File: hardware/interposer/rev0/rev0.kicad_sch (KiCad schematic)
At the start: 14 parts, among them J1 Z80_PLUG_TO_MB, J2 Z80_SOCKET_CPU, J3 5V_INPUT, U1 74AHCT165, U2 74AHCT165, U3 74AHCT165, U4 74AHCT165, U5 PICO_2_W

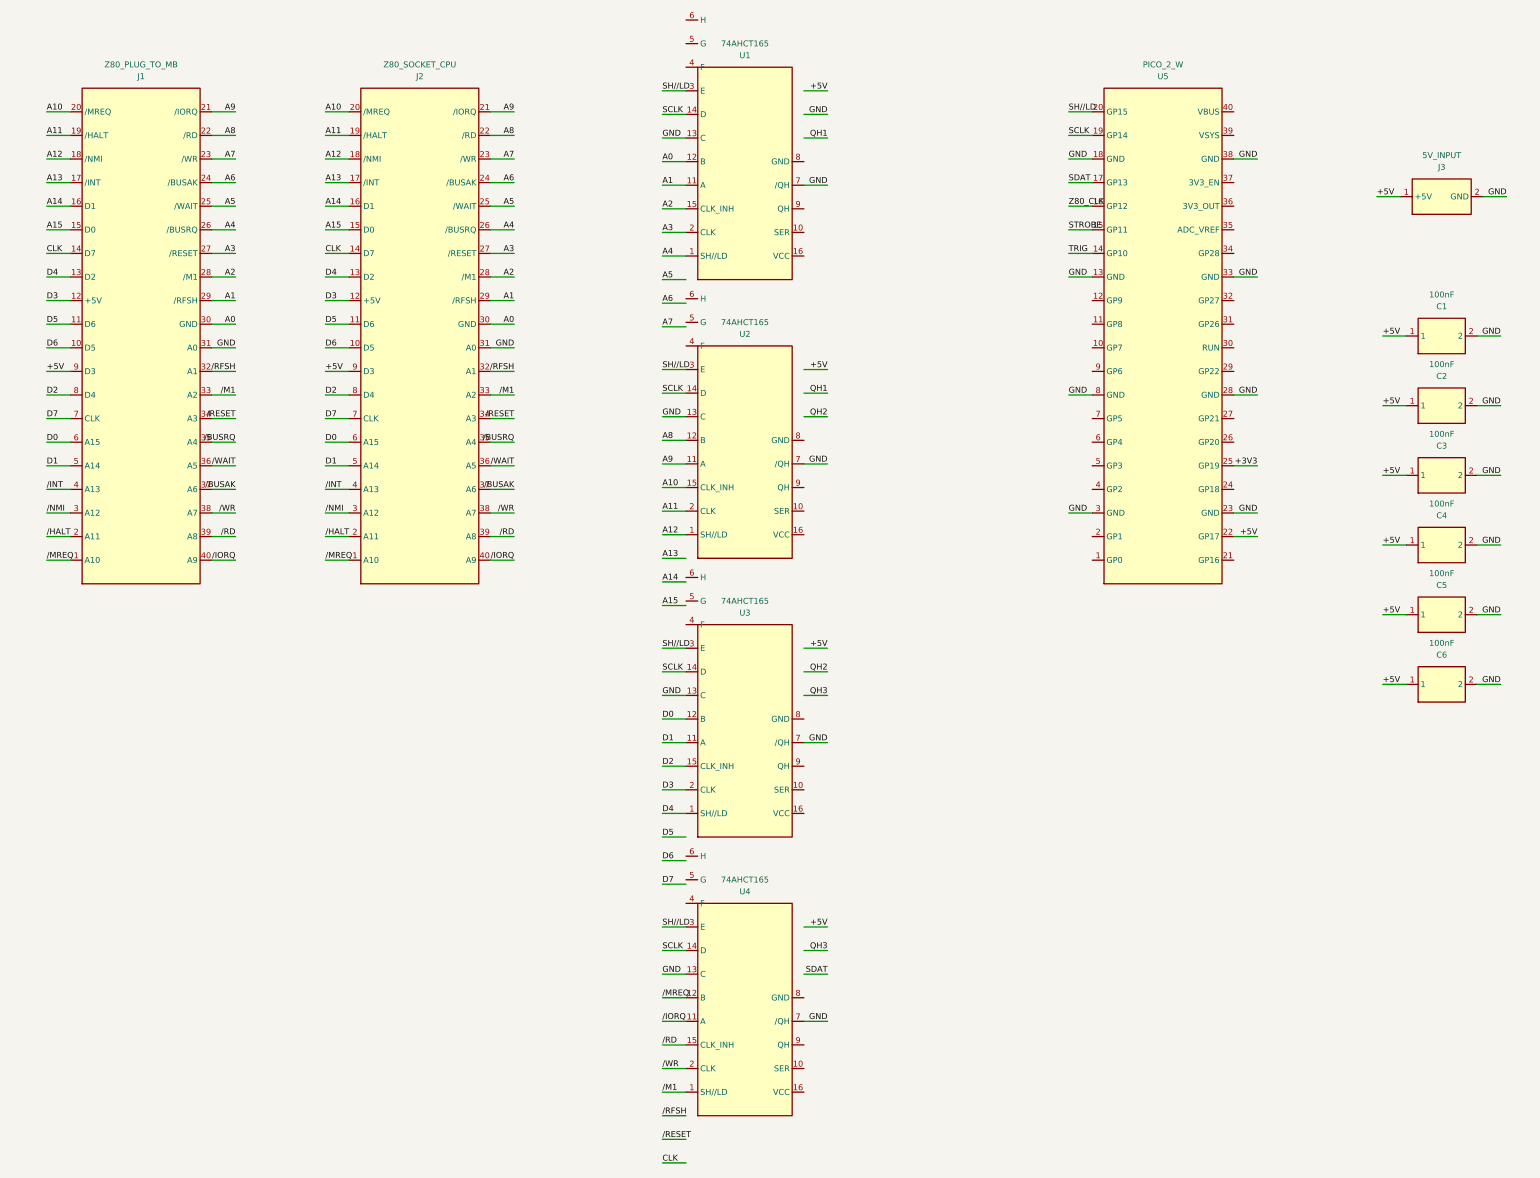
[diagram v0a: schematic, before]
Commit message: hardware: fix mirrored pin placement in interposer schematic generators
The reva/rev0 generators placed a symbol pin at (x + px, y + py), but KiCad
stores symbol geometry Y-up while the sheet is Y-down, so the pin actually
lands at (x + px, y - py).  Every wire stub and net label was therefore
attached to the mirror-image pin and the netlist was broken: reva ERC
reported 93 errors (85 pin_not_connected + 8 label_dangling), rev0 58.

- reva/rev0: correct the Y transform in place(), and make Symbol.pin_pos()/
anchor() use `+hh - off` so `off` really counts down from the top of the box
  (the 'T'/'B' sides were inverted too).  Label justification flipped so the
  text runs away from the symbol body, as in the floppy-adapter generator.
- reva: the 595 drive chain is FOUR devices (U3/U4/U5/U15 -- see SR_OUT), but
  the 165 capture chain also started at y=205, putting U6 directly on top of
  U15.  That shorted SR_RCK/GND, /OE_ADDR/A0, +5V/A1, +5V/A2 and GND/A3 -- the
  netlist reported GND as "A3" with 47 nodes.  Capture chain now starts at 260.
- reva/rev0: snap symbol origins to the 1.27 mm connection grid, and size the
  Z84C00 body 111.76 mm (44 x 1.27) so its pins land on grid.  Verified
  electrically neutral: the exported netlist (nets section) is byte-identical
  with and without the snap.
- reva: fix a stale docstring that claimed to be the Rev 0 generator.

ERC: reva 93 -> 12 errors (565 -> 51 violations), rev0 58 -> 28 (286 -> 46).
The 12/28 remaining are genuinely unused pins (U7/U8 /QH, U11 2A2/2Y2, Pico
RUN/ADC_VREF/3V3_EN/VBUS, ESP32-C3 IO2/IO8/IO10), not geometry faults.  The
residual warnings are `endpoint_off_grid`-free now; what is left is
lib_symbol_issues (no 'local' entry in sym-lib-table -- the symbols are
embedded, so it is cosmetic) and isolated_pin_label on nets that are real
design gaps (/MREQ_DRV, /IORQ_RAW, /Z80_CLK, /ESP_EN, /ESP_BOOT).

Note: gen_lff_sch.py is unaffected -- it emits hierarchical sheets, no pins.

Refs #62.
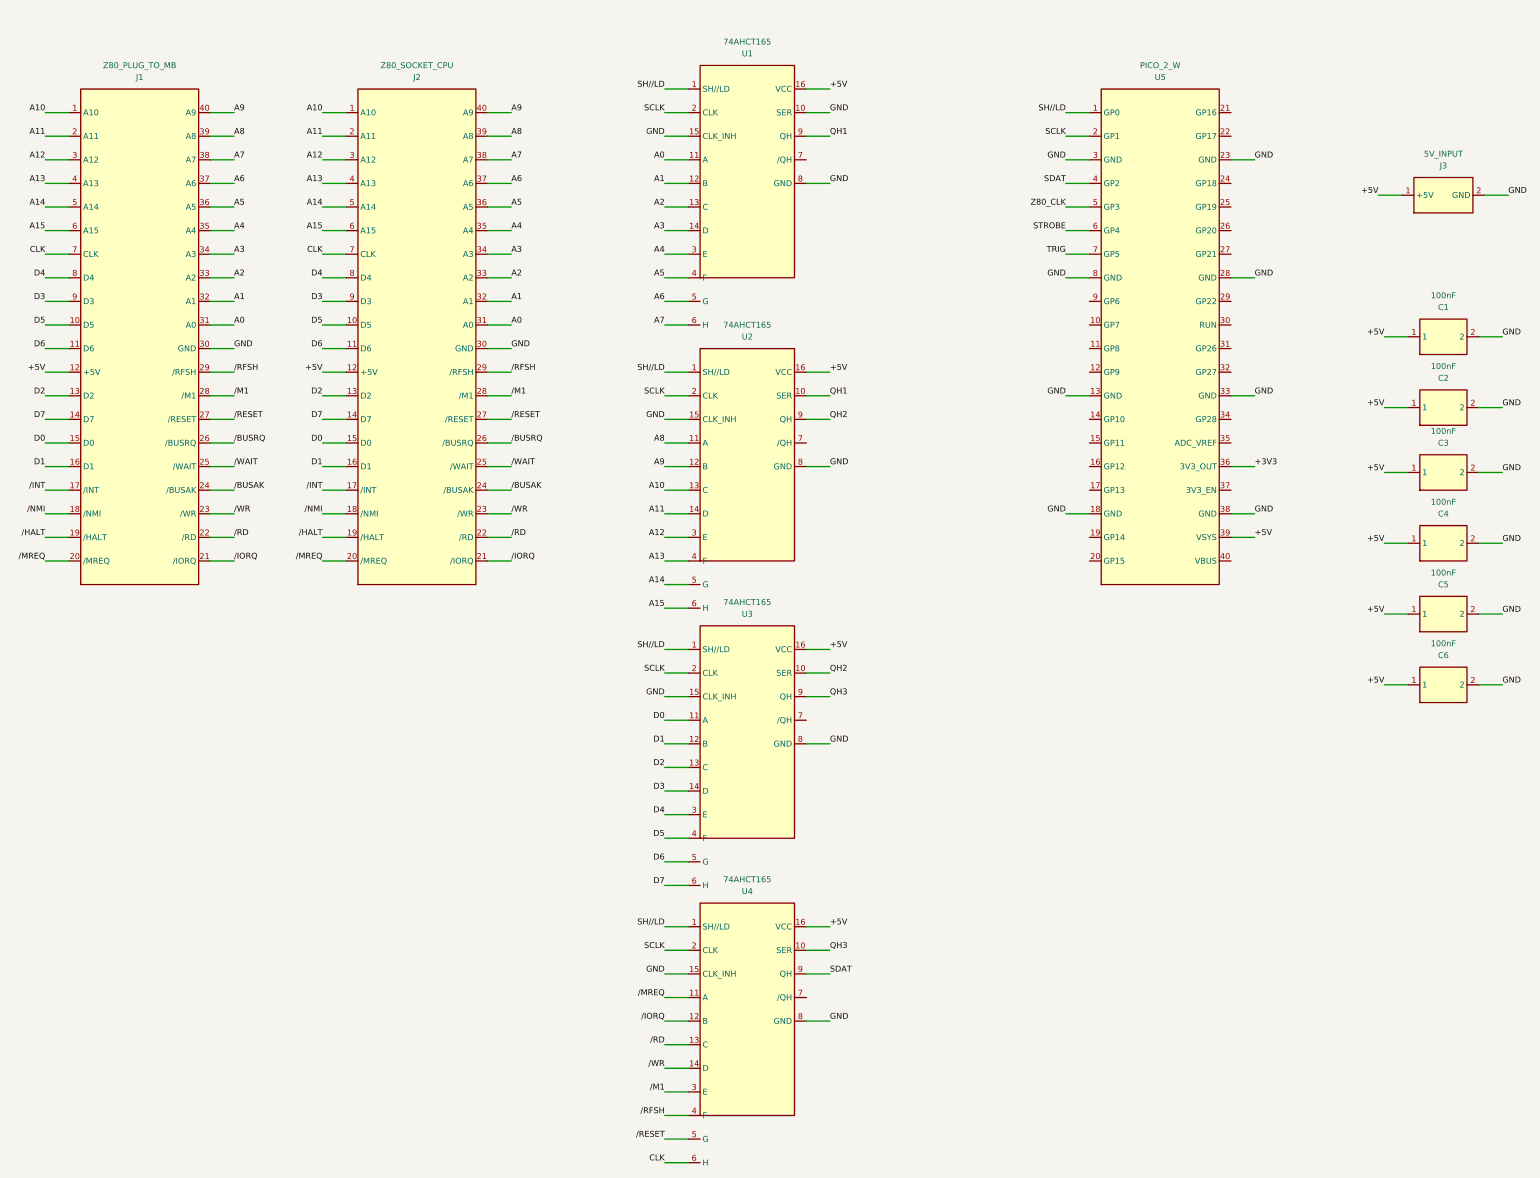
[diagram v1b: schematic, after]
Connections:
- net +3V3: now also U5.36 (3V3_OUT); no longer U5.25 (GP19)
- net +5V: now also J1.12 (+5V), J2.12 (+5V), U1.16 (VCC), U2.16 (VCC), U3.16 (VCC), U4.16 (VCC), U5.39 (VSYS); no longer J1.9 (D3), J2.9 (D3), U5.22 (GP17)
- net /BUSAK: now also J1.24 (/BUSAK), J2.24 (/BUSAK); no longer J1.37 (A6), J2.37 (A6)
- net /BUSRQ: now also J1.26 (/BUSRQ), J2.26 (/BUSRQ); no longer J1.35 (A4), J2.35 (A4)
- net /HALT: now also J1.19 (/HALT), J2.19 (/HALT); no longer J1.2 (A11), J2.2 (A11)
- net /INT: now also J1.17 (/INT), J2.17 (/INT); no longer J1.4 (A13), J2.4 (A13)
- net /IORQ: now also J1.21 (/IORQ), J2.21 (/IORQ), U4.12 (B); no longer J1.40 (A9), J2.40 (A9), U4.11 (A)
- net /M1: now also J1.28 (/M1), J2.28 (/M1), U4.3 (E); no longer J1.33 (A2), J2.33 (A2), U4.1 (SH//LD)
- net /MREQ: now also J1.20 (/MREQ), J2.20 (/MREQ), U4.11 (A); no longer J1.1 (A10), J2.1 (A10), U4.12 (B)
- net /NMI: now also J1.18 (/NMI), J2.18 (/NMI); no longer J1.3 (A12), J2.3 (A12)
- net /RD: now also J1.22 (/RD), J2.22 (/RD), U4.13 (C); no longer J1.39 (A8), J2.39 (A8), U4.15 (CLK_INH)
- net /RESET: now also J1.27 (/RESET), J2.27 (/RESET), U4.5 (G); no longer J1.34 (A3), J2.34 (A3)
- net /RFSH: now also J1.29 (/RFSH), J2.29 (/RFSH), U4.4 (F); no longer J1.32 (A1), J2.32 (A1)
- net /WAIT: now also J1.25 (/WAIT), J2.25 (/WAIT); no longer J1.36 (A5), J2.36 (A5)
- net /WR: now also J1.23 (/WR), J2.23 (/WR), U4.14 (D); no longer J1.38 (A7), J2.38 (A7), U4.2 (CLK)
- net A0: now also J1.31 (A0), J2.31 (A0), U1.11 (A); no longer J1.30 (GND), J2.30 (GND), U1.12 (B)
- net A1: now also J1.32 (A1), J2.32 (A1), U1.12 (B); no longer J1.29 (/RFSH), J2.29 (/RFSH), U1.11 (A)
- net A10: now also J1.1 (A10), J2.1 (A10), U2.13 (C); no longer J1.20 (/MREQ), J2.20 (/MREQ), U2.15 (CLK_INH)
- net A11: now also J1.2 (A11), J2.2 (A11), U2.14 (D); no longer J1.19 (/HALT), J2.19 (/HALT), U2.2 (CLK)
- net A12: now also J1.3 (A12), J2.3 (A12), U2.3 (E); no longer J1.18 (/NMI), J2.18 (/NMI), U2.1 (SH//LD)
- net A13: now also J1.4 (A13), J2.4 (A13), U2.4 (F); no longer J1.17 (/INT), J2.17 (/INT)
- net A14: now also J1.5 (A14), J2.5 (A14), U2.5 (G); no longer J1.16 (D1), J2.16 (D1)
- net A15: now also J1.6 (A15), J2.6 (A15), U2.6 (H); no longer J1.15 (D0), J2.15 (D0)
- net A2: now also J1.33 (A2), J2.33 (A2), U1.13 (C); no longer J1.28 (/M1), J2.28 (/M1), U1.15 (CLK_INH)
- net A3: now also J1.34 (A3), J2.34 (A3), U1.14 (D); no longer J1.27 (/RESET), J2.27 (/RESET), U1.2 (CLK)
- net A4: now also J1.35 (A4), J2.35 (A4), U1.3 (E); no longer J1.26 (/BUSRQ), J2.26 (/BUSRQ), U1.1 (SH//LD)
- net A5: now also J1.36 (A5), J2.36 (A5), U1.4 (F); no longer J1.25 (/WAIT), J2.25 (/WAIT)
- net A6: now also J1.37 (A6), J2.37 (A6), U1.5 (G); no longer J1.24 (/BUSAK), J2.24 (/BUSAK)
- net A7: now also J1.38 (A7), J2.38 (A7), U1.6 (H); no longer J1.23 (/WR), J2.23 (/WR)
- net A8: now also J1.39 (A8), J2.39 (A8), U2.11 (A); no longer J1.22 (/RD), J2.22 (/RD), U2.12 (B)
- net A9: now also J1.40 (A9), J2.40 (A9), U2.12 (B); no longer J1.21 (/IORQ), J2.21 (/IORQ), U2.11 (A)
- net CLK: now also J1.7 (CLK), J2.7 (CLK), U4.6 (H); no longer J1.14 (D7), J2.14 (D7)
- net D0: now also J1.15 (D0), J2.15 (D0), U3.11 (A); no longer J1.6 (A15), J2.6 (A15), U3.12 (B)
- net D1: now also J1.16 (D1), J2.16 (D1), U3.12 (B); no longer J1.5 (A14), J2.5 (A14), U3.11 (A)
- net D2: now also J1.13 (D2), J2.13 (D2), U3.13 (C); no longer J1.8 (D4), J2.8 (D4), U3.15 (CLK_INH)
- net D3: now also J1.9 (D3), J2.9 (D3), U3.14 (D); no longer J1.12 (+5V), J2.12 (+5V), U3.2 (CLK)
- net D4: now also J1.8 (D4), J2.8 (D4), U3.3 (E); no longer J1.13 (D2), J2.13 (D2), U3.1 (SH//LD)
- net D5: now also J1.10 (D5), J2.10 (D5), U3.4 (F); no longer J1.11 (D6), J2.11 (D6)
- net D6: now also J1.11 (D6), J2.11 (D6), U3.5 (G); no longer J1.10 (D5), J2.10 (D5)
- net D7: now also J1.14 (D7), J2.14 (D7), U3.6 (H); no longer J1.7 (CLK), J2.7 (CLK)
- net GND: now also J1.30 (GND), J2.30 (GND), U1.10 (SER), U1.15 (CLK_INH), U1.8 (GND), U2.15 (CLK_INH), U2.8 (GND), U3.15 (CLK_INH), U3.8 (GND), U4.15 (CLK_INH), U4.8 (GND); no longer J1.31 (A0), J2.31 (A0), U1.13 (C), U1.7 (/QH), U2.13 (C), U2.7 (/QH), U3.13 (C), U3.7 (/QH), U4.13 (C), U4.7 (/QH)
- net QH1: now also U1.9 (QH), U2.10 (SER)
- net QH2: now also U2.9 (QH), U3.10 (SER)
- net QH3: now also U3.9 (QH), U4.10 (SER)
- net SCLK: now also U1.2 (CLK), U2.2 (CLK), U3.2 (CLK), U4.2 (CLK), U5.2 (GP1); no longer U1.14 (D), U2.14 (D), U3.14 (D), U4.14 (D), U5.19 (GP14)
- net SDAT: now also U4.9 (QH), U5.4 (GP2); no longer U5.17 (GP13)
- net SH//LD: now also U1.1 (SH//LD), U2.1 (SH//LD), U3.1 (SH//LD), U4.1 (SH//LD), U5.1 (GP0); no longer U1.3 (E), U2.3 (E), U3.3 (E), U4.3 (E), U5.20 (GP15)
- net STROBE: now also U5.6 (GP4); no longer U5.15 (GP11)
- net TRIG: now also U5.7 (GP5); no longer U5.14 (GP10)
- net Z80_CLK: now also U5.5 (GP3); no longer U5.16 (GP12)
